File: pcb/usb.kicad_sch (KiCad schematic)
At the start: 40 parts, among them J6 USB4105-GF-A, J7 S2B-PH-SM4-TB, Q1 DMP3099L-7, Q2 DMG3418L, Q3 DMG3418L, SW1 400MSP1R6BLKM6QE, U149 SN74LVC2G132DCUR, U151 AP2112K-3.3, U152 BQ29700DSER, U153 MCP73831T-2ACI/OT

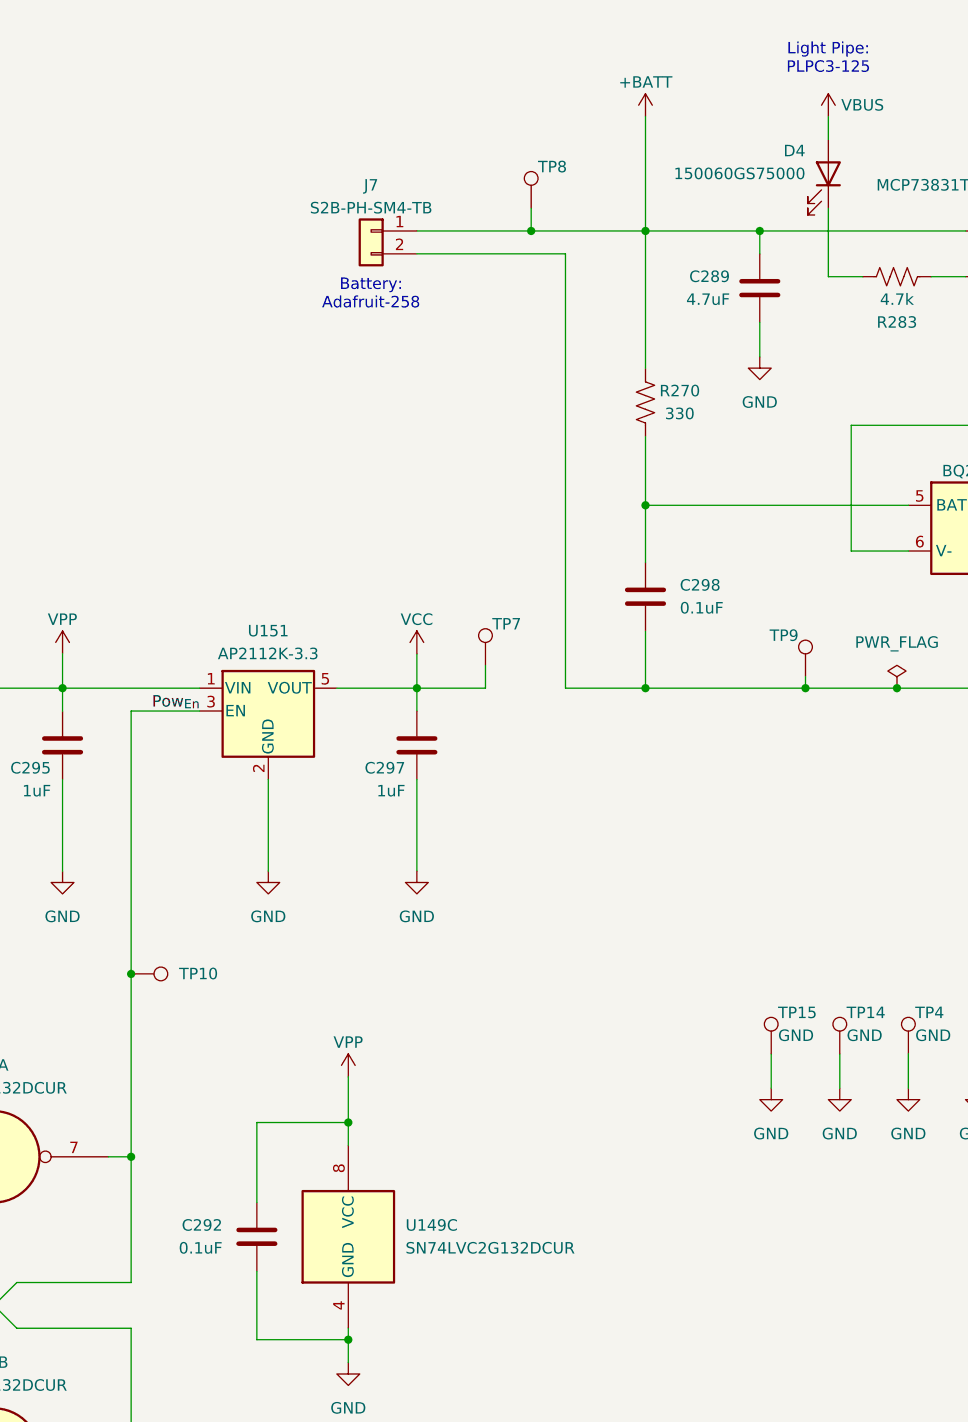
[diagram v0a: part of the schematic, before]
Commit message: 1st step OEPSPN & MPN on components
- still missing new codes to be emitted
- project/schematic/components not tunned with Jon's project at this date
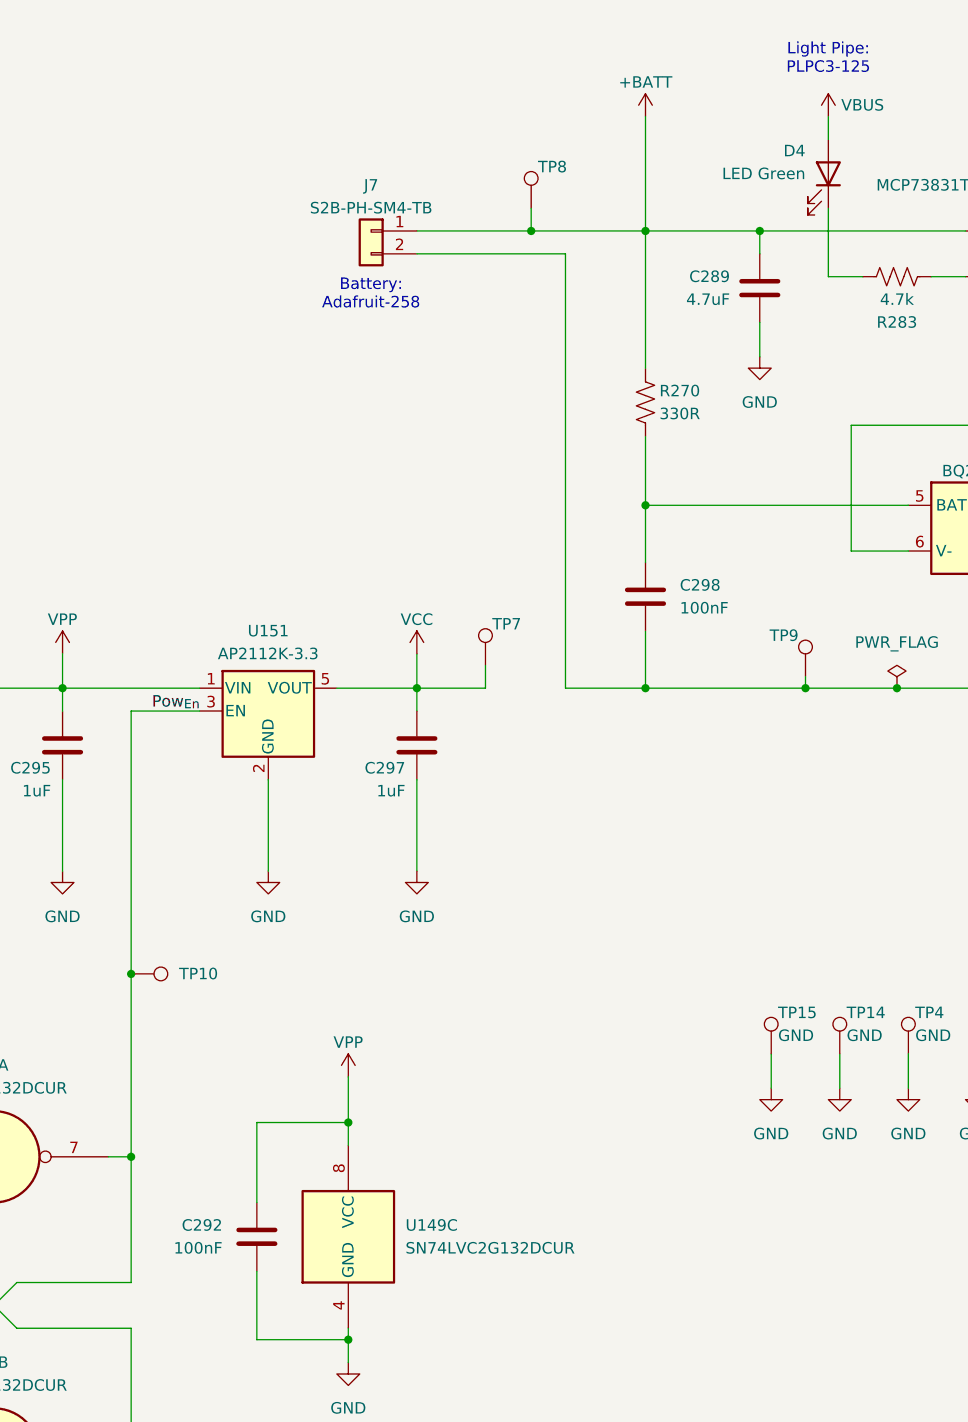
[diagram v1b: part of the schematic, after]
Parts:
- C289: MPN (none) -> CL31B475KOHNNNE; OEPSPN (none) -> OEPS010081
- C292, C298: value 0.1uF -> 100nF; MPN (none) -> C1005X7R1E104K050BB; OEPSPN (none) -> OEPS010050
- C295, C297: MPN (none) -> CL10A105KA8NNNC; OEPSPN (none) -> OEPS010022; Voltage 16V -> 25V
- C299: MPN (none) -> CL31B106KBHNNNE; OEPSPN (none) -> OEPS010032; TempCo X5R -> X7R; Voltage 16V -> 25V
- D3: MPN (none) -> CDBW140-G; OEPSPN (none) -> espera
- D4: value 150060GS75000 -> LED Green; MPN (none) -> 150060GS75000; OEPSPN (none) -> espera
- J6: MPN (none) -> USB4105-GF-A; OEPSPN (none) -> espera
- J7: MPN (none) -> S2B-PH-SM4-TB; OEPSPN (none) -> espera
- Q1: MPN (none) -> DMP3099L-7; OEPSPN (none) -> espera
- Q2, Q3: MPN (none) -> DMG3418L; OEPSPN (none) -> espera
- R263, R264, R265, R268: MPN (none) -> CRCW040210K0FKED; OEPSPN (none) -> OEPS020030
- R266, R267: MPN (none) -> ERJ-2RKF5101X; OEPSPN (none) -> OEPS020173
- R270: value 330 -> 330R; MPN (none) -> RC0402FR-07330RL; OEPSPN (none) -> OEPS020037
- R271, R283: MPN (none) -> ERJ-2RKF4701X; OEPSPN (none) -> OEPS020010
- R272: MPN (none) -> ERJ-2RKF2201X; OEPSPN (none) -> OEPS020174
- SW1: MPN (none) -> 400MSP1R6BLKM6QE; OEPSPN (none) -> espera
- TP1, TP10, TP14, TP15, TP2, TP3, TP4, TP5, TP6, TP7, TP8, TP9: now left out of the parts list
- U149: MPN (none) -> SN74LVC2G132DCUR; OEPSPN (none) -> espera
- U151: MPN (none) -> AP2112K-3.3; OEPSPN (none) -> espera
- U152: MPN (none) -> BQ29700DSER; OEPSPN (none) -> espera
- U153: MPN (none) -> MCP73831T-2ACI/OT; OEPSPN (none) -> espera

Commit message: all OEPSPN
- all components with OEPSPN completed
- this Project Fork version not tunned with Project Main Branch
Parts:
- D3: OEPSPN espera -> OEPS030034
- D4: OEPSPN espera -> OEPS030033
- J6: OEPSPN espera -> OEPS070106
- J7: OEPSPN espera -> OEPS070105
- Q1: OEPSPN espera -> OEPS060020
- Q2, Q3: MPN DMG3418L -> DMG3418L-7; OEPSPN espera -> OEPS060019
- SW1: OEPSPN espera -> OEPS070112
- U149: OEPSPN espera -> OEPS080162
- U151: MPN AP2112K-3.3 -> AP2112K-3.3TRG1; OEPSPN espera -> OEPS080155
- U152: OEPSPN espera -> OEPS080156
- U153: OEPSPN espera -> OEPS080157
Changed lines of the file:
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@@
 			)
 		)
-		(property "OEPSPN" "espera"
+		(property "OEPSPN" "OEPS030033"
 			(at 203.2 43.18 0)
 			(effects
@@
 			)
 		)
-		(property "OEPSPN" "espera"
+		(property "OEPSPN" "OEPS060019"
 			(at 260.35 97.79 0)
 			(effects
@@
 			)
 		)
-		(property "MPN" "DMG3418L"
+		(property "MPN" "DMG3418L-7"
 			(at 260.35 97.79 0)
 			(effects
@@
 			)
 		)
-		(property "OEPSPN" "espera"
+		(property "OEPSPN" "OEPS070106"
 			(at 46.99 46.99 0)
 			(effects
@@
 			)
 		)
-		(property "OEPSPN" "espera"
+		(property "OEPSPN" "OEPS030034"
 			(at 74.93 100.33 0)
 			(effects
@@
 			)
 		)
-		(property "OEPSPN" "espera"
+		(property "OEPSPN" "OEPS060020"
 			(at 82.55 92.71 0)
 			(effects
@@
 			)
 		)
-		(property "OEPSPN" "espera"
+		(property "OEPSPN" "OEPS070105"
 			(at 152.4 49.53 0)
 			(effects
@@
 			)
 		)
-		(property "OEPSPN" "espera"
+		(property "OEPSPN" "OEPS080162"
 			(at 110.49 152.4 0)
 			(effects
@@
 			)
 		)
-		(property "OEPSPN" "espera"
+		(property "OEPSPN" "OEPS080155"
 			(at 140.97 102.87 0)
 			(effects
@@
 			)
 		)
-		(property "MPN" "AP2112K-3.3"
+		(property "MPN" "AP2112K-3.3TRG1"
 			(at 140.97 102.87 0)
 			(effects
@@
 			)
 		)
-		(property "OEPSPN" "espera"
+		(property "OEPSPN" "OEPS080162"
 			(at 149.86 161.29 0)
 			(effects
@@
 			)
 		)
-		(property "OEPSPN" "espera"
+		(property "OEPSPN" "OEPS070112"
 			(at 60.96 161.29 0)
 			(effects
@@
 			)
 		)
-		(property "OEPSPN" "espera"
+		(property "OEPSPN" "OEPS080162"
 			(at 110.49 185.42 0)
 			(effects
@@
 			)
 		)
-		(property "OEPSPN" "espera"
+		(property "OEPSPN" "OEPS080156"
 			(at 222.25 82.55 0)
 			(effects
@@
 			)
 		)
-		(property "OEPSPN" "espera"
+		(property "OEPSPN" "OEPS060019"
 			(at 243.84 97.79 0)
 			(effects
@@
 			)
 		)
-		(property "MPN" "DMG3418L"
+		(property "MPN" "DMG3418L-7"
 			(at 243.84 97.79 0)
 			(effects
@@
 			)
 		)
-		(property "OEPSPN" "espera"
+		(property "OEPSPN" "OEPS080157"
 			(at 228.6 52.07 0)
 			(effects

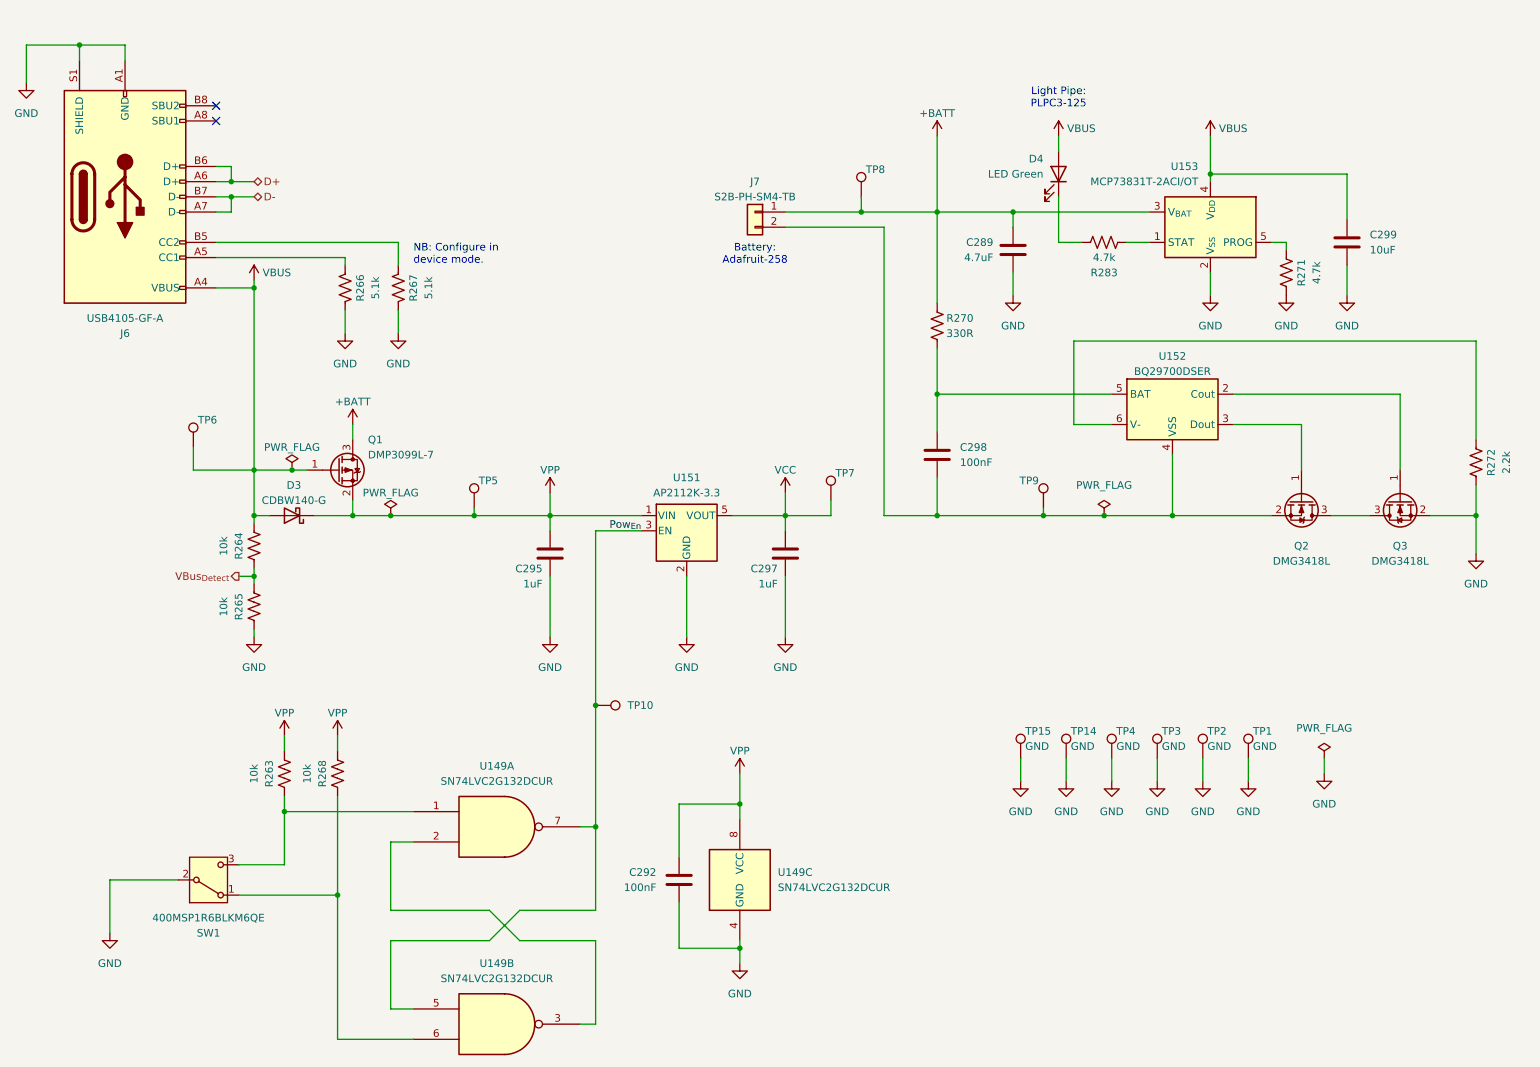
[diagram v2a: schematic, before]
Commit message: tunned with Main branch
- OEPSPN & MPN already on components
- missing 4 these codes
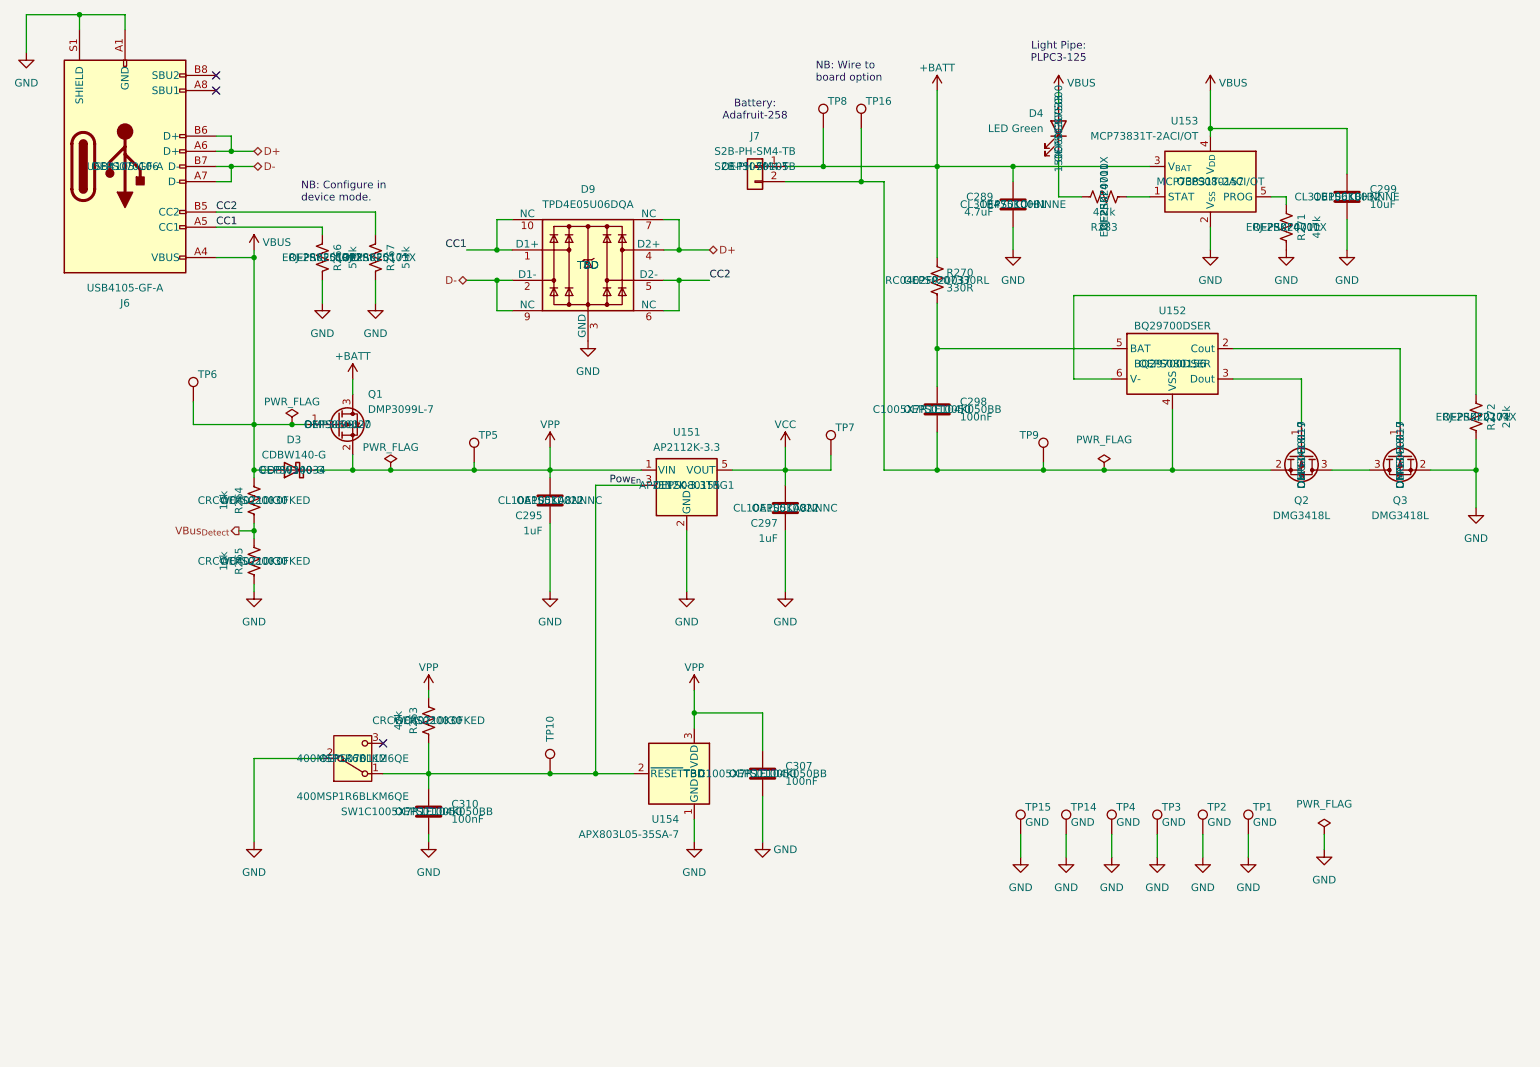
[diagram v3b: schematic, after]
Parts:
- removed C292: 100nF, Capacitor_SMD:C_0402_1005Metric, symbol Device:C
- removed R268: 10k, Resistor_SMD:R_0402_1005Metric, symbol Device:R_US
- removed U149: SN74LVC2G132DCUR, Package_SO:VSSOP-8_2.3x2mm_P0.5mm, symbol 74xGxx:74LVC2G00
- added C307, C310: 100nF, Capacitor_SMD:C_0402_1005Metric, symbol Device:C
- added D9: TPD4E05U06DQA, Package_SON:USON-10_2.5x1.0mm_P0.5mm, symbol Power_Protection:TPD4E05U06DQA
- added TP16: ~, TestPoint:TestPoint_THTPad_D3.0mm_Drill1.5mm, symbol Connector:TestPoint
- added U154: APX803L05-35SA-7, Package_TO_SOT_SMD:SOT-23, symbol Power_Supervisor:TPS3839DBZ
- C295, C297: Voltage 25V -> 16V
- C299: TempCo X7R -> X5R; Voltage 25V -> 16V
- R263: value 10k -> 47k
- TP8: value GND -> ~; footprint TestPoint:TestPoint_Pad_D2.0mm -> TestPoint:TestPoint_THTPad_D3.0mm_Drill1.5mm
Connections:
- net D+: now also D9.4 (D2+), D9.7 (NC)
- net D-: now also D9.2 (D1-), D9.9 (NC)
- net GND: now also C307.2, C310.2, D9.3 (GND), D9.8 (GND), U154.1 (GND)
- net Pow_{En}: now also R263.2, SW1.1 (A), C310.1, U154.2 (~{RESET})
- net VPP: now also C307.1, U154.3 (VDD)
- net CC1: now reaches J6.A5 (CC1), R266.1
- net CC1: now also D9.1 (D1+), D9.10 (NC)
- net CC2: now reaches J6.B5 (CC2), R267.1
- net CC2: now also D9.5 (D2-), D9.6 (NC)
- net at C298.2, J7.2 (Pin_2), Q2.2 (S)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: now also TP16.1
- net at SW1.3 (C): no longer R263.2
- no-connect marks 2 -> 3
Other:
- note added: "NB: Wire to board option"
- moved on the sheet: C289, C295, C297, C298, C299, D3, D4, J6, J7, Q1, Q2, Q3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
